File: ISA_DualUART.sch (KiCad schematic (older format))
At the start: 13 parts, among them J1 ISA BUS, J2 ADDR_IRQ, J3 UART1_SEL, J4 UART2_SEL, J5 Serial 1 IDC, J6 Serial 2 IDC, U1 74LS138, U2 74LS138, U3 16550, U4 16550, U5 GD75232N, U6 GD75232N, X1 1.8432Mhz

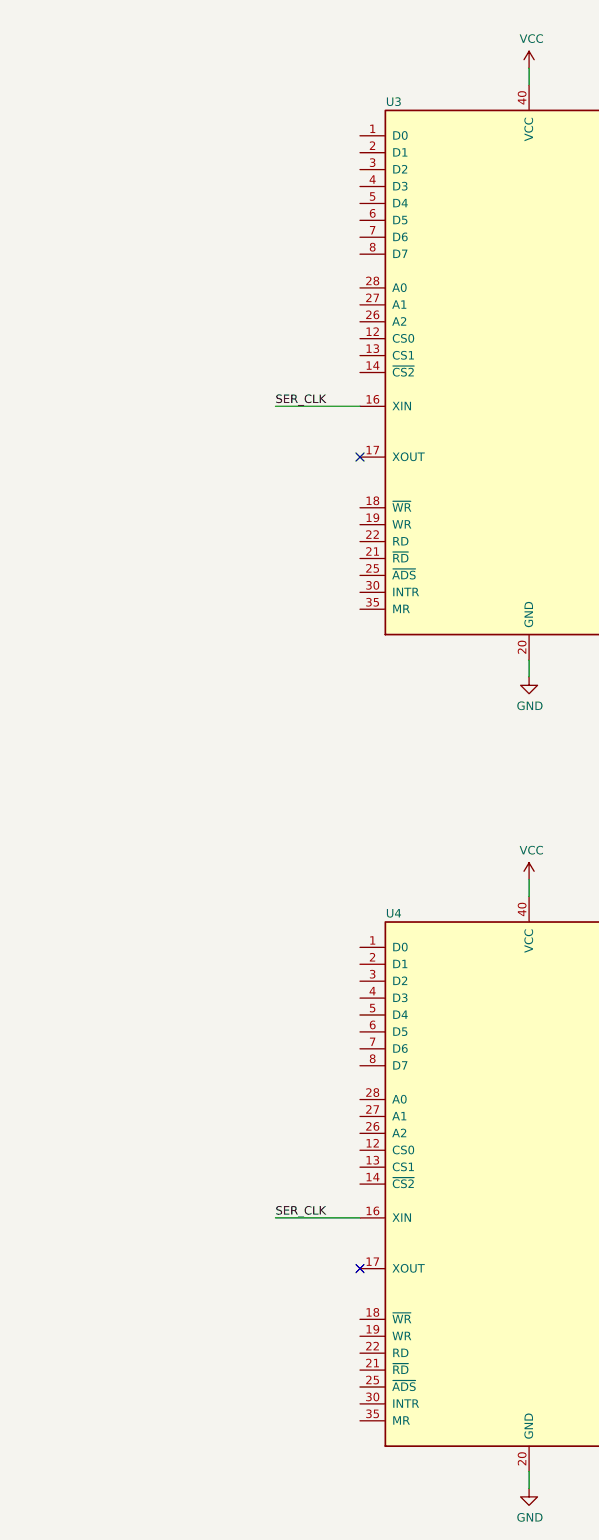
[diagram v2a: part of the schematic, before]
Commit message: Begin wiring UARTs
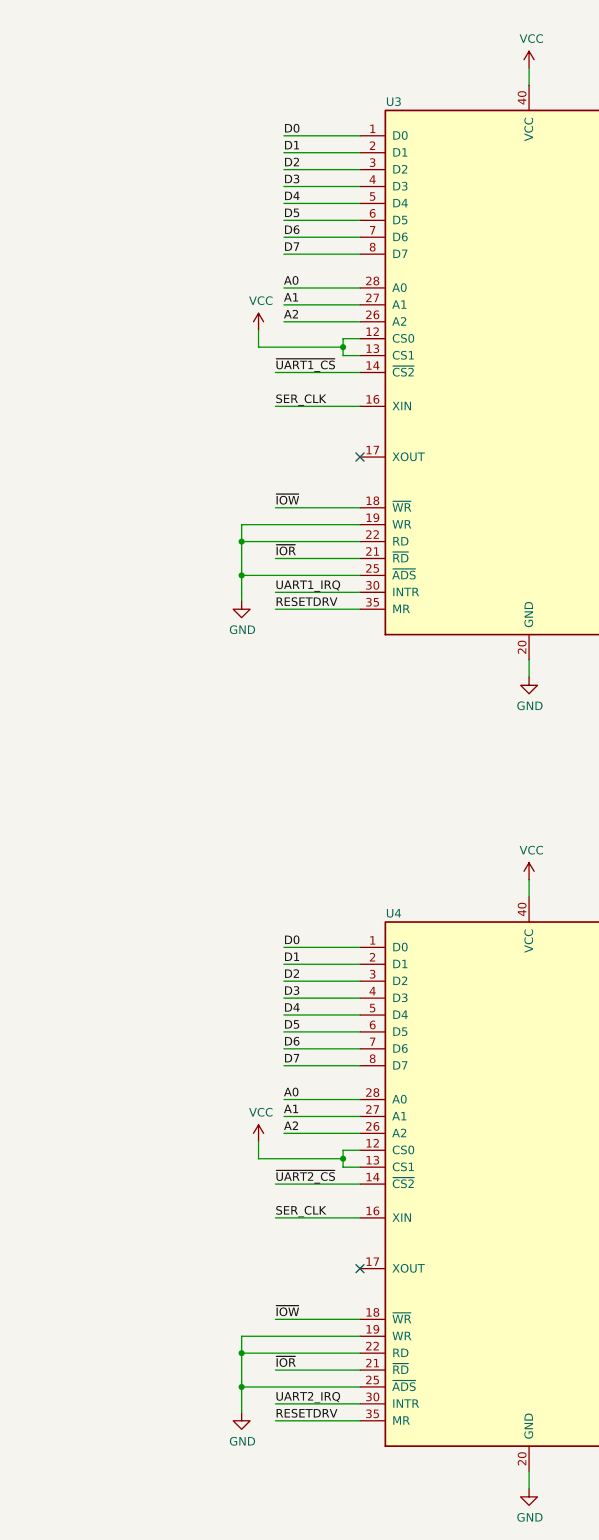
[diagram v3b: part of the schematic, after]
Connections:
- net GND: now also U3.19 (WR), U3.22 (RD), U3.25 (~ADS~), U4.19 (WR), U4.22 (RD), U4.25 (~ADS~)
- net UART1_IRQ: now also U3.30 (INTR)
- net UART2_IRQ: now also U4.30 (INTR)
- net VCC: now also U3.12 (CS0), U3.13 (CS1), U4.12 (CS0), U4.13 (CS1)
- net ~UART1_CS: now also U3.14 (~CS2~)
- net ~UART2_CS: now also U4.14 (~CS2~)
- net D0: now reaches U3.1 (D0)
- net D0: now also U4.1 (D0)
- net ~IOW: now reaches U3.18 (~WR~)
- net ~IOW: now also U4.18 (~WR~)
- net D1: now reaches U3.2 (D1)
- net D1: now also U4.2 (D1)
- net ~IOR: now reaches U3.21 (~RD~)
- net ~IOR: now also U4.21 (~RD~)
- net A2: now reaches U3.26 (A2)
- net A2: now also U4.26 (A2)
- net A1: now reaches U3.27 (A1)
- net A1: now also U4.27 (A1)
- net A0: now reaches U3.28 (A0)
- net A0: now also U4.28 (A0)
- net D2: now reaches U3.3 (D2)
- net D2: now also U4.3 (D2)
- net RESETDRV: now reaches U3.35 (MR)
- net RESETDRV: now also U4.35 (MR)
- net D3: now reaches U3.4 (D3)
- net D3: now also U4.4 (D3)
- net D4: now reaches U3.5 (D4)
- net D4: now also U4.5 (D4)
- net D5: now reaches U3.6 (D5)
- net D5: now also U4.6 (D5)
- net D6: now reaches U3.7 (D6)
- net D6: now also U4.7 (D6)
- net D7: now reaches U3.8 (D7)
- net D7: now also U4.8 (D7)
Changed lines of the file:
@@
 Wire Wire Line
 	10050 4800 10050 4900
+Wire Wire Line
+	6100 3000 6000 3000
+Wire Wire Line
+	6000 3000 6000 2950
+Wire Wire Line
+	6000 2900 6100 2900
+Wire Wire Line
+	6000 2950 5500 2950
+Wire Wire Line
+	5500 2950 5500 2850
+Connection ~ 6000 2950
+Wire Wire Line
+	6000 2950 6000 2900
+$Comp
+L power:VCC #PWR?
+U 1 1 6019347C
+P 5500 2850
+F 0 "#PWR?" H 5500 2700 50  0001 C CNN
+F 1 "VCC" H 5515 3023 50  0000 C CNN
+F 2 "" H 5500 2850 50  0001 C CNN
+F 3 "" H 5500 2850 50  0001 C CNN
+	1    5500 2850
+	1    0    0    -1
+$EndComp
+Wire Wire Line
+	6100 3100 5600 3100
+Text Label 5600 3100 0    50   ~ 0
+~UART1_CS
+Wire Wire Line
+	6100 7800 6000 7800
+Wire Wire Line
+	6000 7800 6000 7750
+Wire Wire Line
+	6000 7700 6100 7700
+Wire Wire Line
+	6000 7750 5500 7750
+Wire Wire Line
+	5500 7750 5500 7650
+Connection ~ 6000 7750
+Wire Wire Line
+	6000 7750 6000 7700
+$Comp
+L power:VCC #PWR?
+U 1 1 6019BCF3
+P 5500 7650
+F 0 "#PWR?" H 5500 7500 50  0001 C CNN
+F 1 "VCC" H 5515 7823 50  0000 C CNN
+F 2 "" H 5500 7650 50  0001 C CNN
+F 3 "" H 5500 7650 50  0001 C CNN
+	1    5500 7650
+	1    0    0    -1
+$EndComp
+Wire Wire Line
+	6100 7900 5600 7900
+Text Label 5600 7900 0    50   ~ 0
+~UART2_CS
+Wire Wire Line
+	6100 6500 5650 6500
+Wire Wire Line
+	6100 6600 5650 6600
+Wire Wire Line
+	6100 6700 5650 6700
+Wire Wire Line
+	6100 6800 5650 6800
+Wire Wire Line
+	6100 6900 5650 6900
+Wire Wire Line
+	6100 7000 5650 7000
+Wire Wire Line
+	6100 7100 5650 7100
+Wire Wire Line
+	6100 7200 5650 7200
+Text Label 5650 6500 0    50   ~ 0
+D0
+Text Label 5650 6600 0    50   ~ 0
+D1
+Text Label 5650 6700 0    50   ~ 0
+D2
+Text Label 5650 6800 0    50   ~ 0
+D3
+Text Label 5650 6900 0    50   ~ 0
+D4
+Text Label 5650 7000 0    50   ~ 0
+D5
+Text Label 5650 7100 0    50   ~ 0
+D6
+Text Label 5650 7200 0    50   ~ 0
+D7
+Wire Wire Line
+	6100 7400 5650 7400
+Wire Wire Line
+	6100 7500 5650 7500
+Wire Wire Line
+	6100 7600 5650 7600
+Text Label 5650 7400 0    50   ~ 0
+A0
+Text Label 5650 7500 0    50   ~ 0
+A1
+Text Label 5650 7600 0    50   ~ 0
+A2
+Wire Wire Line
+	6100 1700 5650 1700
+Wire Wire Line
+	6100 1800 5650 1800
+Wire Wire Line
+	6100 1900 5650 1900
+Wire Wire Line
+	6100 2000 5650 2000
+Wire Wire Line
+	6100 2100 5650 2100
+Wire Wire Line
+	6100 2200 5650 2200
+Wire Wire Line
+	6100 2300 5650 2300
+Wire Wire Line
+	6100 2400 5650 2400
+Text Label 5650 1700 0    50   ~ 0
+D0
+Text Label 5650 1800 0    50   ~ 0
+D1
+Text Label 5650 1900 0    50   ~ 0
+D2
+Text Label 5650 2000 0    50   ~ 0
+D3
+Text Label 5650 2100 0    50   ~ 0
+D4
+Text Label 5650 2200 0    50   ~ 0
+D5
+Text Label 5650 2300 0    50   ~ 0
+D6
+Text Label 5650 2400 0    50   ~ 0
+D7
+Wire Wire Line
+	6100 2600 5650 2600
+Wire Wire Line
+	6100 2700 5650 2700
+Wire Wire Line
+	6100 2800 5650 2800
+Text Label 5650 2600 0    50   ~ 0
+A0
+Text Label 5650 2700 0    50   ~ 0
+A1
+Text Label 5650 2800 0    50   ~ 0
+A2
+Text Label 5600 4500 0    50   ~ 0
+RESETDRV
+Text Label 5600 4400 0    50   ~ 0
+UART1_IRQ
+Wire Wire Line
+	5600 4400 6100 4400
+Wire Wire Line
+	5600 4500 6100 4500
+Wire Wire Line
+	6100 4200 5600 4200
+Text Label 5600 4200 0    50   ~ 0
+~IOR
+Wire Wire Line
+	6100 3900 5600 3900
+Text Label 5600 3900 0    50   ~ 0
+~IOW
+Wire Wire Line
+	6100 4000 5400 4000
+Wire Wire Line
+	5400 4000 5400 4100
+Wire Wire Line
+	5400 4100 6100 4100
+Wire Wire Line
+	6100 4300 5400 4300
+Wire Wire Line
+	5400 4300 5400 4100
+Connection ~ 5400 4100
+$Comp
+L power:GND #PWR?
+U 1 1 60233DB3
+P 5400 4450
+F 0 "#PWR?" H 5400 4200 50  0001 C CNN
+F 1 "GND" H 5405 4277 50  0000 C CNN
+F 2 "" H 5400 4450 50  0001 C CNN
+F 3 "" H 5400 4450 50  0001 C CNN
+	1    5400 4450
+	1    0    0    -1
+$EndComp
+Wire Wire Line
+	5400 4300 5400 4450
+Connection ~ 5400 4300
+Text Label 5600 9300 0    50   ~ 0
+RESETDRV
+Text Label 5600 9200 0    50   ~ 0
+UART2_IRQ
+Wire Wire Line
+	5600 9200 6100 9200
+Wire Wire Line
+	5600 9300 6100 9300
+Wire Wire Line
+	6100 9000 5600 9000
+Text Label 5600 9000 0    50   ~ 0
+~IOR
+Wire Wire Line
+	6100 8700 5600 8700
+Text Label 5600 8700 0    50   ~ 0
+~IOW
+Wire Wire Line
+	6100 8800 5400 8800
+Wire Wire Line
+	5400 8800 5400 8900
+Wire Wire Line
+	5400 8900 6100 8900
+Wire Wire Line
+	6100 9100 5400 9100
+Wire Wire Line
+	5400 9100 5400 8900
+Connection ~ 5400 8900
+$Comp
+L power:GND #PWR?
+U 1 1 6023ADAB
+P 5400 9250
+F 0 "#PWR?" H 5400 9000 50  0001 C CNN
+F 1 "GND" H 5405 9077 50  0000 C CNN
+F 2 "" H 5400 9250 50  0001 C CNN
+F 3 "" H 5400 9250 50  0001 C CNN
+	1    5400 9250
+	1    0    0    -1
+$EndComp
+Wire Wire Line
+	5400 9100 5400 9250
+Connection ~ 5400 9100
 $EndSCHEMATC

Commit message: First revision of the schematic
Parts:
- added C1, C3, C5, C6: 10uF, Capacitor_THT:CP_Radial_D5.0mm_P2.50mm, symbol Device:CP_Small
- added C10, C11, C12, C13, C2, C4, C7, C8, C9: 100nF, Capacitor_THT:C_Disc_D6.0mm_W2.5mm_P5.00mm, symbol Device:C_Small
- added D1: LED RX1, LED_THT:LED_D3.0mm, symbol Device:LED_Small
- added D2: LED TX1, LED_THT:LED_D3.0mm, symbol Device:LED_Small
- added D3: LED RX2, LED_THT:LED_D3.0mm, symbol Device:LED_Small
- added D4: LED TX2, LED_THT:LED_D3.0mm, symbol Device:LED_Small
- added J7: Serial 1 DB9, Connector_Dsub:DSUB-9_Male_Horizontal_P2.77x2.84mm_EdgePinOffset4.94mm_Housed_MountingHolesOffset7.48mm, symbol Connector:DB9_Male
- added R1, R2, R3, R4: 1k, Resistor_THT:R_Axial_DIN0207_L6.3mm_D2.5mm_P10.16mm_Horizontal, symbol Device:R_Small
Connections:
- net +12V: now also J1.9 (+12V), C3.1, C4.1
- net -12V: now also J1.7 (-12V), C1.2, C2.2
- net A0: now also J1.62 (BA00)
- net A1: now also J1.61 (BA01)
- net A2: now also J1.60 (BA02)
- net A3: now also J1.59 (BA03)
- net A4: now also J1.58 (BA04)
- net A5: now also J1.57 (BA05)
- net A6: now also J1.56 (BA06)
- net A7: now also J1.55 (BA07)
- net A8: now also J1.54 (BA08)
- net A9: now also J1.53 (BA09)
- net AEN: now also J1.42 (AEN)
- net D0: now also J1.40 (DB0)
- net D1: now also J1.39 (DB1)
- net D2: now also J1.38 (DB2)
- net D3: now also J1.37 (DB3)
- net D4: now also J1.36 (DB4)
- net D5: now also J1.35 (DB5)
- net D6: now also J1.34 (DB6)
- net D7: now also J1.33 (DB7)
- net GND: now also J1.1 (GND), J1.10 (GND), J1.31 (GND), J5.5 (Pin_5), J6.5 (Pin_5), C1.1, C10.2, C11.2, C12.2, C13.2, C2.1, C3.2, C4.2, C5.2, C6.2, C7.2, C8.2, C9.2, J7.5
- net IRQ3: now also J1.25 (IRQ3)
- net IRQ4: now also J1.24 (IRQ4)
- net IRQ5: now also J1.23 (IRQ5)
- net IRQ7: now also J1.21 (IRQ7)
- net RESETDRV: now also J1.2 (RESET)
- net VCC: now also J1.29 (VCC), J1.3 (VCC), C10.1, C11.1, C12.1, C13.1, C5.1, C6.1, C7.1, C8.1, C9.1, R1.2, R2.2, R3.2, R4.2
- net ~IOR: now also J1.14 (~IOR)
- net ~IOW: now also J1.13 (~IOW)
- net ~MEMW: now reaches J1.11 (~SMEMW)
- net ~MEMR: now reaches J1.12 (~SMEMR)
- net IRQ6: now reaches J1.22 (IRQ6)
- net ~DACK2: now reaches J1.26 (~DACK2)
- net TC: now reaches J1.27 (TC)
- net A19: now reaches J1.43 (BA19)
- net A18: now reaches J1.44 (BA18)
- net A17: now reaches J1.45 (BA17)
- net A16: now reaches J1.46 (BA16)
- net A15: now reaches J1.47 (BA15)
- net A14: now reaches J1.48 (BA14)
- net A13: now reaches J1.49 (BA13)
- net A12: now reaches J1.50 (BA12)
- net A11: now reaches J1.51 (BA11)
- net A10: now reaches J1.52 (BA10)
- net DRQ2: now reaches J1.6 (DRQ2)
- net ~RI_1: now reaches U5.12 (RY5)
- net ~RI_1: now also U3.39 (~RI~)
- net ~DTR_1: now reaches U5.13 (DA3)
- net ~DTR_1: now also U3.33 (~DTR~)
- net ~CTS_1: now reaches U5.14 (RY4)
- net ~CTS_1: now also U3.36 (~CTS~)
- net SOUT_1: now reaches U5.15 (DA2)
- net SOUT_1: now also U3.11 (SOUT), D2.1 (K)
- net ~RTS_1: now reaches U5.16 (DA1)
- net ~RTS_1: now also U3.32 (~RTS~)
- net SIN_1: now reaches U5.17 (RY3)
- net SIN_1: now also U3.10 (SIN), D1.1 (K)
- net ~DSR_1: now reaches U5.18 (RY2)
- net ~DSR_1: now also U3.37 (~DSR~)
- net ~DCD_1: now reaches U5.19 (RY1)
- net ~DCD_1: now also U3.38 (~DCD~)
- net RS232_1_DCD: now reaches U5.2 (RA1)
- net RS232_1_DCD: now also J5.1 (Pin_1), J7.1
- net RS232_1_DSR: now reaches U5.3 (RA2)
- net RS232_1_DSR: now also J5.6 (Pin_6), J7.6
- net RS232_1_RX: now reaches U5.4 (RA3)
- net RS232_1_RX: now also J5.2 (Pin_2), J7.2
- net RS232_1_RTS: now reaches U5.5 (DY1)
- net RS232_1_RTS: now also J5.7 (Pin_7), J7.7
- net RS232_1_TX: now reaches U5.6 (DY2)
- net RS232_1_TX: now also J5.3 (Pin_3), J7.3
- net RS232_1_CTS: now reaches U5.7 (RA4)
- net RS232_1_CTS: now also J5.8 (Pin_8), J7.8
- net RS232_1_DTR: now reaches U5.8 (DY3)
- net RS232_1_DTR: now also J5.4 (Pin_4), J7.4
- net RS232_1_RI: now reaches U5.9 (RA5)
- net RS232_1_RI: now also J5.9 (Pin_9), J7.9
- net at U3.15 (~BAUDOUT~): now also U3.9 (RCLK)
- net ~RI_2: now reaches U6.12 (RY5)
- net ~RI_2: now also U4.39 (~RI~)
- net ~DTR_2: now reaches U6.13 (DA3)
- net ~DTR_2: now also U4.33 (~DTR~)
- net ~CTS_2: now reaches U6.14 (RY4)
- net ~CTS_2: now also U4.36 (~CTS~)
- net SOUT_2: now reaches U6.15 (DA2)
- net SOUT_2: now also U4.11 (SOUT), D4.1 (K)
- net ~RTS_2: now reaches U6.16 (DA1)
- net ~RTS_2: now also U4.32 (~RTS~)
- net SIN_2: now reaches U6.17 (RY3)
- net SIN_2: now also U4.10 (SIN), D3.1 (K)
- net ~DSR_2: now reaches U6.18 (RY2)
- net ~DSR_2: now also U4.37 (~DSR~)
- net ~DCD_2: now reaches U6.19 (RY1)
- net ~DCD_2: now also U4.38 (~DCD~)
- net RS232_2_DCD: now reaches U6.2 (RA1)
- net RS232_2_DCD: now also J6.1 (Pin_1)
- net RS232_2_DSR: now reaches U6.3 (RA2)
- net RS232_2_DSR: now also J6.6 (Pin_6)
- net RS232_2_RX: now reaches U6.4 (RA3)
- net RS232_2_RX: now also J6.2 (Pin_2)
- net RS232_2_RTS: now reaches U6.5 (DY1)
- net RS232_2_RTS: now also J6.7 (Pin_7)
- net RS232_2_TX: now reaches U6.6 (DY2)
- net RS232_2_TX: now also J6.3 (Pin_3)
- net RS232_2_CTS: now reaches U6.7 (RA4)
- net RS232_2_CTS: now also J6.8 (Pin_8)
- net RS232_2_DTR: now reaches U6.8 (DY3)
- net RS232_2_DTR: now also J6.4 (Pin_4)
- net RS232_2_RI: now reaches U6.9 (RA5)
- net RS232_2_RI: now also J6.9 (Pin_9)
- net at U4.15 (~BAUDOUT~): now also U4.9 (RCLK)
- new net: D1.2 (A), R1.1
- new net: D2.2 (A), R2.1
- new net: D3.2 (A), R3.1
- new net: D4.2 (A), R4.1
- no-connect marks 14 -> 39
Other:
- moved on the sheet: J1, J6

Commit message: Add gameport circuit
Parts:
- added C14, C15, C16, C17: 51p, Capacitor_THT:C_Disc_D5.0mm_W2.5mm_P2.50mm, symbol Device:C_Small
- added RN1: 10k, Resistor_THT:R_Array_SIP9, symbol Device:R_Network08
- added RN2: 4.7k, Resistor_THT:R_Array_SIP9, symbol Device:R_Network08
- added SW1: GP Address, symbol skiselev_libraries:Switch_DIP_8_Positions
- added U10: 74LS32, Package_DIP:DIP-14_W7.62mm_LongPads, symbol 74xx:74LS32
- added unit 2 of U3
- added U7: NE558, Package_DIP:DIP-16_W7.62mm_Socket_LongPads, symbol skiselev_libraries:NE558
- added U8: 74LS688, Package_DIP:DIP-20_W7.62mm_LongPads, symbol 74xx:74LS688
- added U9: 74HC244, Package_DIP:DIP-20_W7.62mm_LongPads, symbol 74xx:74HC244
- U3: value 16550 -> 74LS32; footprint Package_DIP:DIP-40_W15.24mm_LongPads -> Package_DIP:DIP-14_W7.62mm_LongPads
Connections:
- net A2: now also U8.2 (P0)
- net A3: now also U8.4 (P1)
- net A4: now also U8.6 (P2)
- net A5: now also U8.8 (P3)
- net A6: now also U8.11 (P4)
- net A7: now also U8.13 (P5)
- net A8: now also U8.15 (P6)
- net A9: now also U8.17 (P7)
- net AEN: now also U8.1 (G)
- net D0: now also U9.18 (1Y0)
- net D1: now also U9.16 (1Y1)
- net D2: now also U9.14 (1Y2)
- net D3: now also U9.12 (1Y3)
- net D4: now also U9.9 (2Y3)
- net D5: now also U9.7 (2Y2)
- net D6: now also U9.5 (2Y1)
- net D7: now also U9.3 (2Y0)
- net GND: now also C14.2, C15.2, C16.2, C17.2, RN1.1 (common), U7.12 (GND), U8.10 (GND), U9.10 (GND)
- net VCC: now also RN2.1 (common), SW1.1, SW1.2, SW1.3, SW1.4, SW1.5, SW1.6, SW1.7, SW1.8, U7.5 (VCC), U8.20 (VCC), U9.20 (VCC)
- net ~IOR: now also U3.5
- net ~IOW: now also U10.1
- new net: RN1.5 (R4), SW1.12, U8.12 (R4)
- new net: RN1.4 (R3), SW1.11, U8.14 (R5)
- new net: RN1.3 (R2), SW1.10, U8.16 (R6)
- new net: RN1.2 (R1), SW1.9, U8.18 (R7)
- new net: U10.2, U3.4, U8.19 (P=R)
- new net: RN1.9 (R8), SW1.16, U8.3 (R0)
- new net: RN1.8 (R7), SW1.15, U8.5 (R1)
- new net: RN1.7 (R6), SW1.14, U8.7 (R2)
- new net: RN1.6 (R5), SW1.13, U8.9 (R3)
- new net: U3.6, U9.1 (1OE), U9.19 (2OE)
- new net J1B1: C14.1, RN2.2 (R1), U9.11 (2A3)
- new net J1B2: C15.1, RN2.3 (R2), U9.13 (2A2)
- new net J1X0: RN2.9 (R8), U9.2 (1A0)
- new net J1Y0: RN2.8 (R7), U9.4 (1A1)
- new net J2B1: C16.1, RN2.4 (R3), U9.15 (2A1)
- new net J2B2: C17.1, RN2.5 (R4), U9.17 (2A0)
- new net J2X0: RN2.7 (R6), U9.6 (1A2)
- new net J2Y0: RN2.6 (R5), U9.8 (1A3)
- new net J_TRIG: U10.3
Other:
- moved on the sheet: C10, C11, C12, C13, C5, C6, C7, C8, C9, D1, D2, D3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
